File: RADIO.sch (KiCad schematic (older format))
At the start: 20 parts, among them Q501 MMBF170, U501 SN74AVC2T244, U502 SN74AVC2T244, U503 SN74AVC2T244, U504 A7, U505 SIM_SLOT, U506 SN74AVC2T244

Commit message: This branch moves from i.mx7 to STM32F4 CPU to be finished for Hackaday Prize 2017
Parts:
- Q501: symbol MMBF170 -> MMBF170-RESCUE-3210retro
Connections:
- net labels added: HST_RX, HST_TX
- net labels removed: AT_UART0, AT_UART1, AT_UART2, AT_UART3, AT_UART[0..3], HST_DL0, HST_DL1, HST_DL[0..1]
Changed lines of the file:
@@
 EESchema Schematic File Version 2
+LIBS:3210retro-rescue
 LIBS:a7
 LIBS:ft232rl
@@
 LIBS:contrib
 LIBS:valves
+LIBS:stm32
 LIBS:3210retro-cache
-EELAYER 25 0
+EELAYER 26 0
 EELAYER END
 $Descr A3 16535 11693
 encoding utf-8
-Sheet 5 13
+Sheet 5 10
 Title "Nokia 3210 Retrofit"
 Date "2017-06-15"
@@
 $EndComp
 Wire Wire Line
-	2400 6950 4000 6950
-Wire Wire Line
-	2400 6850 4000 6850
-Wire Wire Line
-	2400 4400 4000 4400
-Wire Wire Line
-	2400 5750 4000 5750
-Wire Wire Line
-	2400 5650 4000 5650
-Wire Wire Line
-	2400 4500 4000 4500
+	2950 6950 4000 6950
+Wire Wire Line
+	2950 6850 4000 6850
+Wire Wire Line
+	2950 4400 4000 4400
+Wire Wire Line
+	2950 5750 4000 5750
+Wire Wire Line
+	2950 5650 4000 5650
+Wire Wire Line
+	2950 4500 4000 4500
 Text HLabel 8050 4350 0    60   Input ~ 0
 ON
@@
 Wire Wire Line
 	7500 4550 8850 4550
-Text HLabel 1950 4100 0    60   BiDi ~ 0
-AT_UART[0..3]
-Entry Wire Line
-	2300 4300 2400 4400
-Entry Wire Line
-	2300 5650 2400 5750
-Entry Wire Line
-	2300 5550 2400 5650
-Entry Wire Line
-	2300 4400 2400 4500
-Wire Bus Line
-	2300 4100 2300 5650
-Wire Bus Line
-	2300 4100 1950 4100
-Text Label 2400 4400 0    60   ~ 0
-AT_UART2
-Text Label 2400 4500 0    60   ~ 0
-AT_UART3
-Text Label 2400 5650 0    60   ~ 0
-AT_UART1
-Text Label 2400 5750 0    60   ~ 0
-AT_UART0
-Entry Wire Line
-	2300 6850 2400 6950
-Entry Wire Line
-	2300 6750 2400 6850
-Text Label 2400 6850 0    60   ~ 0
-HST_DL0
-Text Label 2400 6950 0    60   ~ 0
-HST_DL1
-Wire Bus Line
-	2300 6600 2300 6850
-Wire Bus Line
-	2300 6600 2100 6600
-Text HLabel 2100 6600 0    60   BiDi ~ 0
-HST_DL[0..1]
-$Comp
-L MMBF170 Q501
+Text Label 3100 6850 0    60   ~ 0
+HST_RX
+Text Label 3100 6950 0    60   ~ 0
+HST_TX
+$Comp
+L MMBF170-RESCUE-3210retro Q501
 U 1 1 5942BF1F
 P 6950 3900
+AR Path="/5942BF1F" Ref="Q501"  Part="1"
+AR Path="/5805F481/5942BF1F" Ref="Q501"  Part="1"
 F 0 "Q501" H 7150 3975 50  0000 L CNN
 F 1 "MMBF170" H 7150 3900 50  0000 L CNN
@@
 Wire Wire Line
 	5600 4850 5600 4400
+Text Label 3100 4500 0    60   ~ 0
+AT_UART_CTS
 Text Label 3100 4400 0    60   ~ 0
-AT_UART_CTS
-Text Label 3100 4500 0    60   ~ 0
 AT_UART_RTS
+Text Label 3100 5750 0    60   ~ 0
+AT_UART_RX
 Text Label 3100 5650 0    60   ~ 0
-AT_UART_RX
-Text Label 3100 5750 0    60   ~ 0
 AT_UART_TX
 $Comp
@@
 	1    0    0    -1
 $EndComp
+Text HLabel 2950 4500 0    60   Output ~ 0
+AT_UART_CTS
+Text HLabel 2950 4400 0    60   Input ~ 0
+AT_UART_RTS
+Text HLabel 2950 5750 0    60   Input ~ 0
+AT_UART_RX
+Text HLabel 2950 5650 0    60   Output ~ 0
+AT_UART_TX
+Text HLabel 2950 6850 0    60   Input ~ 0
+HST_RX
+Text HLabel 2950 6950 0    60   Output ~ 0
+HST_TX
 $EndSCHEMATC

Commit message: Modification for STM32 adaption
For the Hackaday Prize 2017 I decided to switch to STM32 as CPU

*Power system was modified to just contain the charge IC,
*Boost converter for high voltage peripherals
*Buck converter for 3V3 for CPU and switchable NVCC_3V3
   for peripherie

CPU signals are routed and pinmux is done in firmware folder.

SD-Card has 4bit Interface

WiFi module ESP8266 is connected via UART

Wolfson Ausio codec is connected via SAI

Two digital microphones for noise canceling

Rumble Motor driver

LCD is connected via it's own I2C interface
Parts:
- C501, C503, C504, C505, C506, C507: footprint Capacitors_SMD:C_0402 -> Capacitors_SMD:C_0402_NoSilk
- R501, R502, R503, R504, R505: footprint Resistors_SMD:R_0402 -> Resistors_SMD:R_0402_NoSilk
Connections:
- net labels added: 4V_BST
- net labels removed: +4V
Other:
- moved on the sheet: C501, C502, C503, C504, C505, C506, C507, Q501, R501, R502, R503, R504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

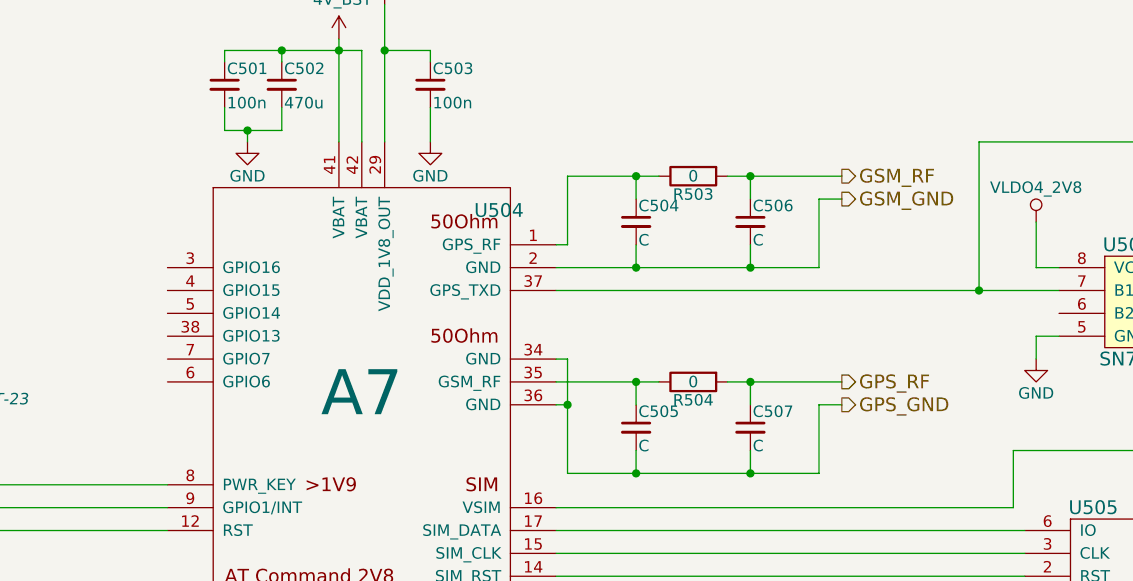
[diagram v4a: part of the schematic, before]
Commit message: Placed a lot of components and routed the audio codec
The BGA of tha audio chipset is to small for regualr technology.
We do not use all of the pins of the chip so we ignore the other
pads and escape throug the balls of the other pad.
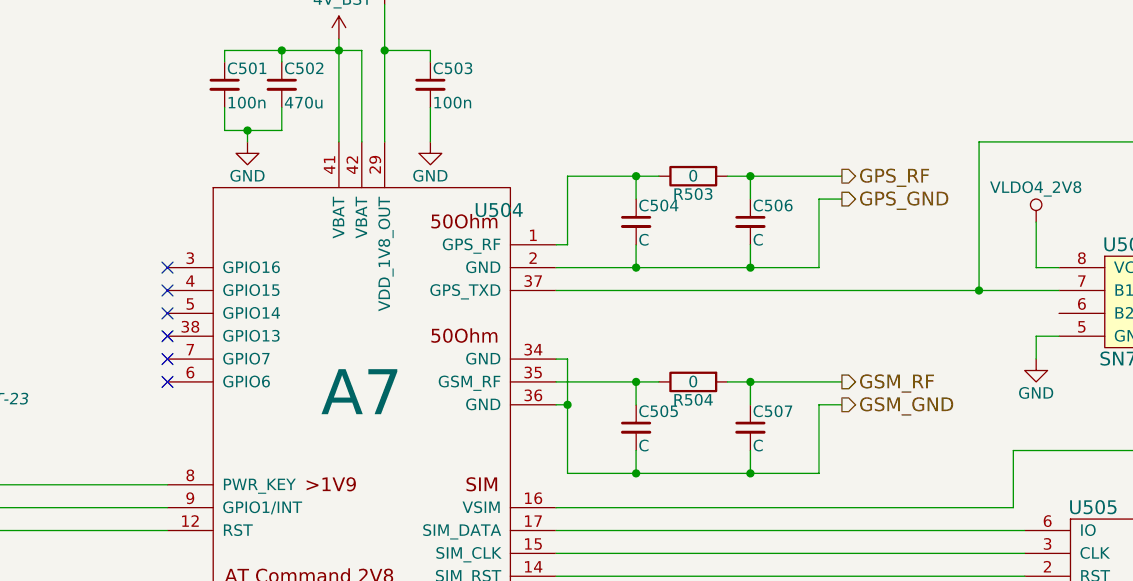
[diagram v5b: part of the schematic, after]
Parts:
- U501, U502, U503, U506: footprint (none) -> NokiaRetroFit:SN74AVC2T244
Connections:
- net GPS_GND: now also C504.2, C506.2, U504.2 (GND); no longer C505.2, C507.2, U504.34 (GND), U504.36 (GND)
- net GPS_RF: now also C506.1, R503.2; no longer C507.1, R504.2
- net GSM_GND: now also C505.2, C507.2, U504.34 (GND), U504.36 (GND); no longer C504.2, C506.2, U504.2 (GND)
- net GSM_RF: now also C507.1, R504.2; no longer C506.1, R503.2
- no-connect marks 0 -> 6
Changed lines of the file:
@@
 LIBS:contrib
 LIBS:valves
-LIBS:tps62742
-LIBS:WM8994ECS
+LIBS:stm32
 LIBS:3210retro-cache
 EELAYER 26 0
@@
 Comment4 ""
 $EndDescr
-Text HLabel 7900 1900 2    60   Output ~ 0
+Text HLabel 7900 2800 2    60   Output ~ 0
 GSM_GND
-Text HLabel 7900 2700 2    60   Output ~ 0
+Text HLabel 7900 1800 2    60   Output ~ 0
 GPS_RF
 $Comp
@@
 	7000 2700 7000 2800
 Connection ~ 7000 2700
-Text HLabel 7900 2800 2    60   Output ~ 0
+Text HLabel 7900 1900 2    60   Output ~ 0
 GPS_GND
 Wire Wire Line
@@
 	7500 3100 7500 3000
 Connection ~ 7500 3100
-Text HLabel 7900 1800 2    60   Output ~ 0
+Text HLabel 7900 2700 2    60   Output ~ 0
 GSM_RF
 $Comp
@@
 F 0 "U501" H 2900 4750 60  0000 C CNN
 F 1 "SN74AVC2T244" H 2700 4250 60  0000 C CNN
-F 2 "" H 2700 4500 60  0001 C CNN
+F 2 "NokiaRetroFit:SN74AVC2T244" H 2700 4500 60  0001 C CNN
 F 3 "" H 2700 4500 60  0001 C CNN
 	1    2700 4500
@@
 F 0 "U502" H 2900 6100 60  0000 C CNN
 F 1 "SN74AVC2T244" H 2700 5600 60  0000 C CNN
-F 2 "" H 2700 5850 60  0001 C CNN
+F 2 "NokiaRetroFit:SN74AVC2T244" H 2700 5850 60  0001 C CNN
 F 3 "" H 2700 5850 60  0001 C CNN
 	1    2700 5850
@@
 F 0 "U503" H 2900 7200 60  0000 C CNN
 F 1 "SN74AVC2T244" H 2700 6700 60  0000 C CNN
-F 2 "" H 2700 6950 60  0001 C CNN
+F 2 "NokiaRetroFit:SN74AVC2T244" H 2700 6950 60  0001 C CNN
 F 3 "" H 2700 6950 60  0001 C CNN
 	1    2700 6950
@@
 F 0 "U506" H 9550 2600 60  0000 C CNN
 F 1 "SN74AVC2T244" H 9350 2100 60  0000 C CNN
-F 2 "" H 9350 2350 60  0001 C CNN
+F 2 "NokiaRetroFit:SN74AVC2T244" H 9350 2350 60  0001 C CNN
 F 3 "" H 9350 2350 60  0001 C CNN
 	1    9350 2350
@@
 Wire Wire Line
 	3600 4450 3600 3650
+NoConn ~ 4950 2200
+NoConn ~ 4950 2300
+NoConn ~ 4950 2400
+NoConn ~ 4950 2500
+NoConn ~ 4950 2600
+NoConn ~ 4950 2700
 $EndSCHEMATC

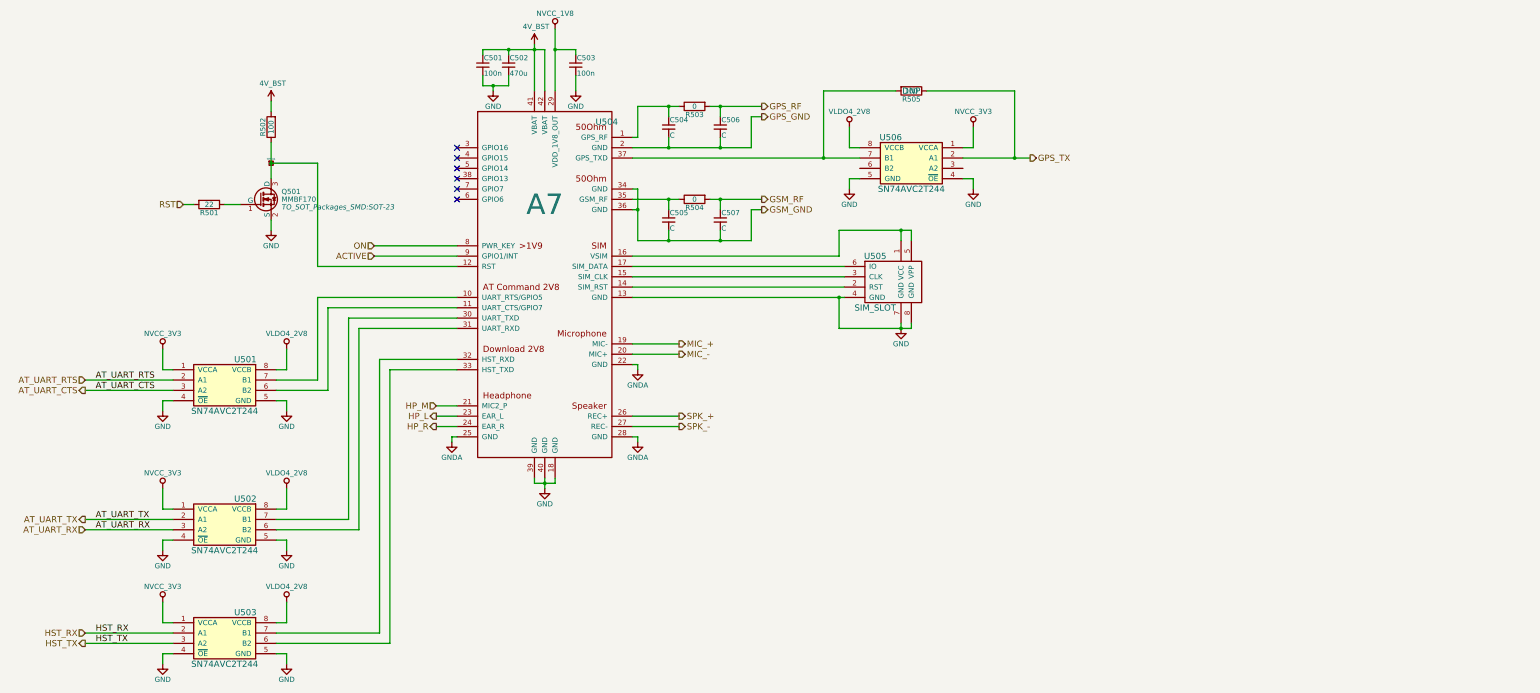
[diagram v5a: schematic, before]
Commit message: Revision 1 of Layout
6layer board
through-hole via only (0.5/0.3mm drill)
0.2mm track width

https://hackaday.io/project/21263-nokia-3210-retro-fit-board/log/66914-prototype-pcb-done-there-comes-the-review
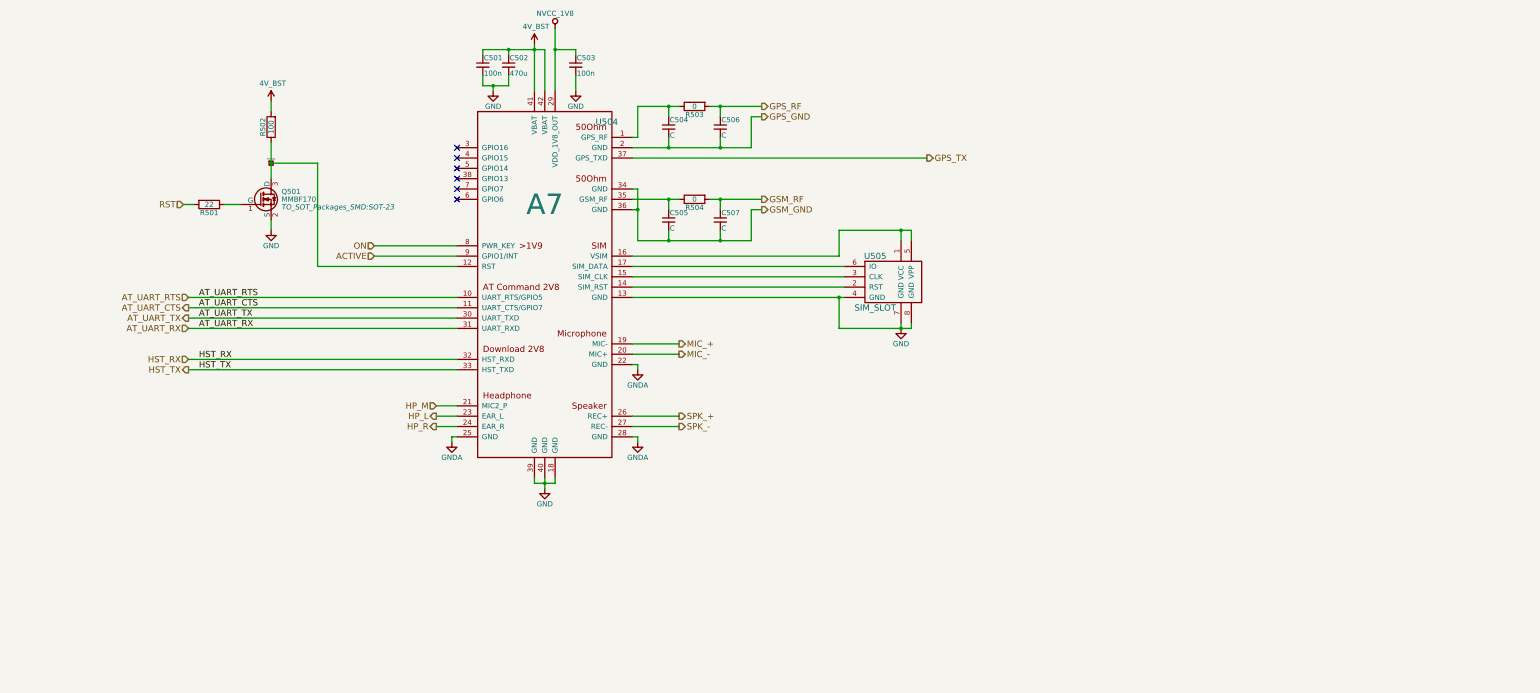
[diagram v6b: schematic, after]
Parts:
- removed R505: 100, Resistors_SMD:R_0402_NoSilk, symbol R
- removed U501, U502, U503, U506: SN74AVC2T244, NokiaRetroFit:SN74AVC2T244, symbol SN74AVC2T244
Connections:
- net AT_UART_CTS: now also U504.11 (UART_CTS/GPIO7)
- net AT_UART_RTS: now also U504.10 (UART_RTS/GPIO5)
- net AT_UART_RX: now also U504.31 (UART_RXD)
- net AT_UART_TX: now also U504.30 (UART_TXD)
- net GPS_TX: now also U504.37 (GPS_TXD)
- net HST_RX: now also U504.32 (HST_RXD)
- net HST_TX: now also U504.33 (HST_TXD)

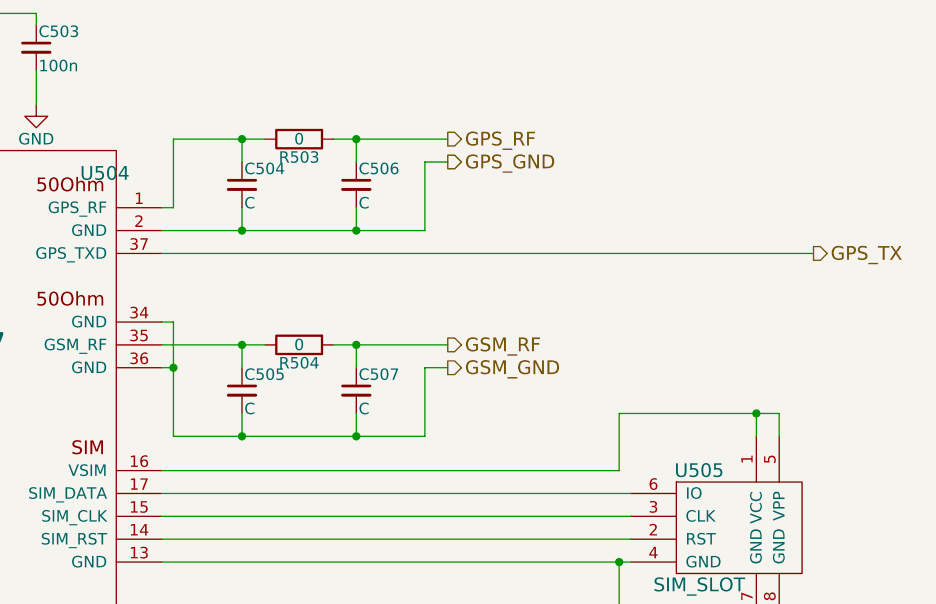
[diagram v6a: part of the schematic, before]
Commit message: Board modified to actual measurements
* rumble motor was on the wrong side of the board. fixed
* some drill holes where missing
* moved voice mic to bottom side. top side is completely
  enclosed by the case
* several small fixes
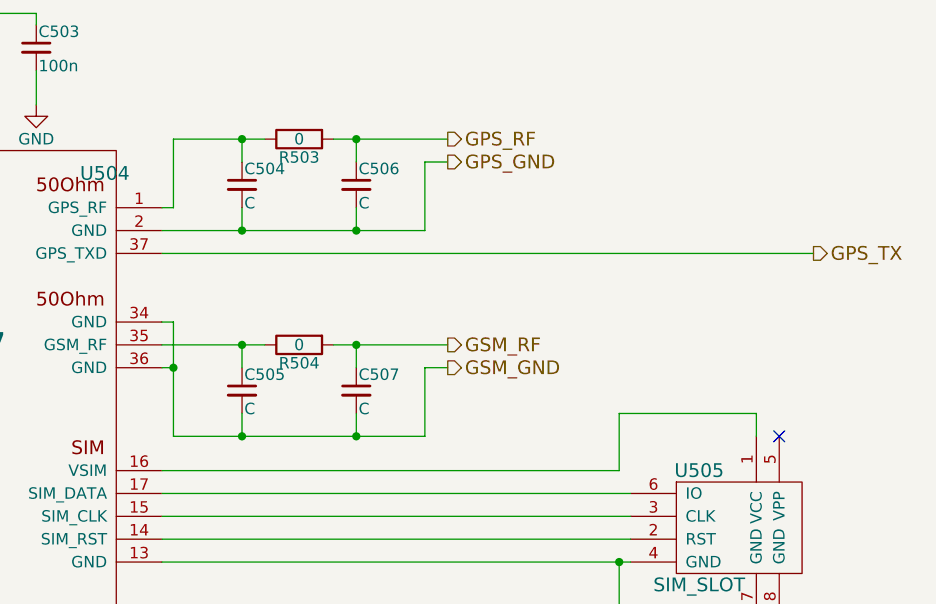
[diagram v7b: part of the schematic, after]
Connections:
- net at U504.16 (VSIM), U505.1 (VCC): no longer U505.5 (VPP)
- no-connect marks 6 -> 7
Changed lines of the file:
@@
 LIBS:contrib
 LIBS:valves
-LIBS:stm32
+LIBS:tps62742
+LIBS:WM8994ECS
 LIBS:3210retro-cache
 EELAYER 26 0
@@
 	7900 2800 7800 2800
 Wire Wire Line
-	7800 2800 7800 3100
+	7800 3100 7800 2800
 Wire Wire Line
 	6700 2600 6700 3100
@@
 	7900 1900 7800 1900
 Wire Wire Line
-	7800 1900 7800 2200
-Wire Wire Line
-	7800 2200 6650 2200
+	7800 2200 7800 1900
+Wire Wire Line
+	6650 2200 7800 2200
 Wire Wire Line
 	7000 2100 7000 2200
@@
 	8650 3250 8650 3000
 Wire Wire Line
-	8650 3000 9350 3000
+	8650 3000 9250 3000
 Wire Wire Line
 	9250 3000 9250 3100
-Wire Wire Line
-	9350 3000 9350 3100
-Connection ~ 9250 3000
 Wire Wire Line
 	9250 3900 9250 3950
@@
 NoConn ~ 4950 2600
 NoConn ~ 4950 2700
+NoConn ~ 9350 3100
 $EndSCHEMATC
